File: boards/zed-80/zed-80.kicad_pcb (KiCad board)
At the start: 2 copper layers, 31 parts, among them J401 TYPE-C-31-M-12, SW201 SW_Push, U201 GD74LS04, U202 Z84C0010PEC, U301 TT74LS32BI, U302 AT28C256-15PU, U303 HM628128BLP-10, U401 CH340C, U402 MC68B50P, Y201 7.3728 MHz

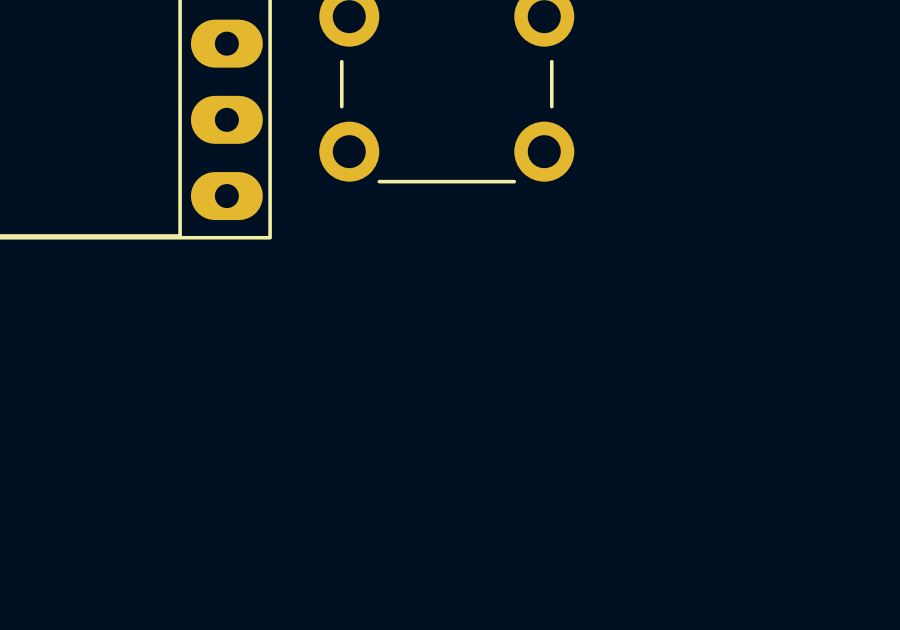
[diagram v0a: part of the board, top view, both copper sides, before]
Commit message: New zed-80 revision and initial ROM programmer schematic
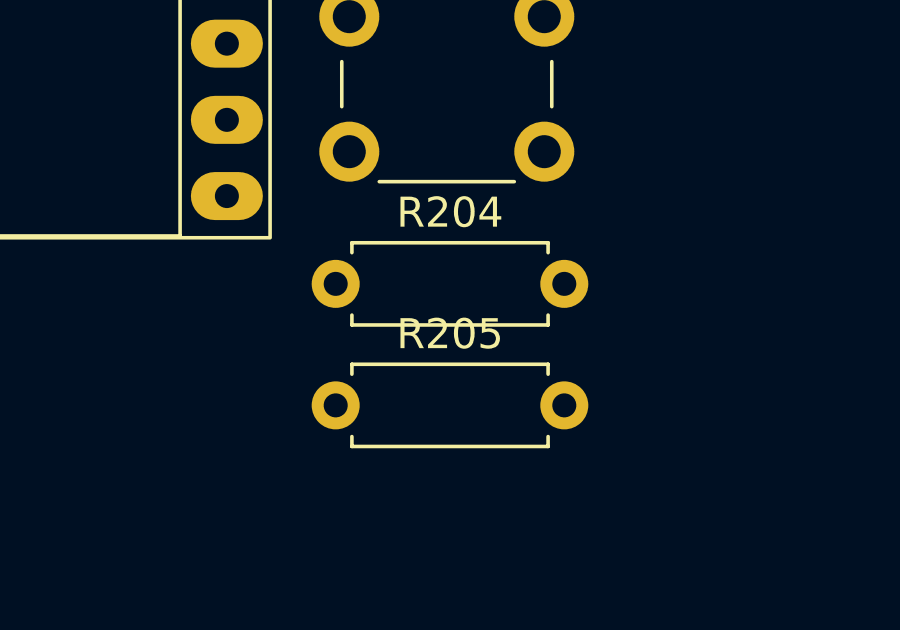
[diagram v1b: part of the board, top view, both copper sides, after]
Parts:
- added R204: 10 kΩ, Resistor_THT:R_Axial_DIN0207_L6.3mm_D2.5mm_P7.62mm_Horizontal, F.Cu at (104.9, 101.5)
- added R205: 1 kΩ, Resistor_THT:R_Axial_DIN0207_L6.3mm_D2.5mm_P7.62mm_Horizontal, F.Cu at (104.9, 105.5)
- R201: value 1 MΩ -> 2 kΩ
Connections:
- U401 pad 15: unconnected-(U401-R232-Pad15) -> GND
- U402 pad 23: unconnected-(U402-~{DCD}-Pad23) -> GND
- U402 pad 24: unconnected-(U402-~{CTS}-Pad24) -> GND

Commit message: Initial layout for main board
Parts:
- moved MH101 97.5 mm to (85.0, 45.0)
- moved J401 84.4 mm to (82.4, 71.2), turned to -90 degrees
- moved MH103 82.9 mm to (85.0, 107.5)
- moved D401 77.1 mm to (84.2, 82.2), turned to -90 degrees
- moved R401 75.0 mm to (83.8, 63.6), turned to 90 degrees
- moved R402 73.5 mm to (88.8, 63.6), turned to 90 degrees
- moved U401 66.6 mm to (95.0, 71.5), turned to -90 degrees
- moved R403 62.5 mm to (91.2, 83.2)
- moved MH102 61.2 mm to (182.5, 45.0)
- moved C402 60.6 mm to (94.0, 66.0)
- moved U301 59.5 mm to (120.2, 89.4)
- moved R203 58.1 mm to (169.1, 93.0), turned to 180 degrees
- moved SW201 56.9 mm to (162.0, 97.5)
- moved U202 56.3 mm to (142.3, 51.4)
- moved C401 54.5 mm to (93.5, 77.2)
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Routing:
- net /CPU/A0: track 0.00 -> 63.3 mm
- net /CPU/A6: track 0.00 -> 42.2 mm
- net /CPU/A4: track 0.00 -> 42.2 mm
- net /CPU/A2: track 0.00 -> 42.2 mm
- net /CPU/A5: track 0.00 -> 42.2 mm
- net /CPU/A1: track 0.00 -> 42.2 mm
- net /CPU/A3: track 0.00 -> 42.2 mm
- net Net-(C201-Pad1): track 0.00 -> 33.3 mm
- net /CPU/D1: track 0.00 -> 21.1 mm
- net /CPU/D0: track 0.00 -> 21.1 mm
- net /CPU/A8: track 0.00 -> 21.1 mm
- net /CPU/CLK: track 0.00 -> 14.2 mm
- net Net-(C202-Pad1): track 0.00 -> 13.1 mm
- net Net-(R201-Pad2): track 0.00 -> 9.56 mm
- net /CPU/A7: track 0.00 -> 5.96 mm
- added copper zone on B.Cu, net GND
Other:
- board outline added: 107.5 x 72.5 mm

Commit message: Initial PCB design for main board
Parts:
- moved U302 39.2 mm to (161.1, 56.5)
- moved U301 39.2 mm to (155.6, 106.1), turned to 90 degrees
- moved C302 35.7 mm to (168.5, 51.5)
- moved R204 28.6 mm to (110.9, 84.8), turned to 0 degrees
- moved C301 27.5 mm to (160.2, 93.5), turned to 180 degrees
- moved U303 20.8 mm to (141.6, 51.5)
- moved U202 20.1 mm to (122.1, 51.4)
- moved C203 20.0 mm to (121.7, 103.2)
- moved SW201 19.5 mm to (142.5, 98.5)
- moved R203 19.5 mm to (149.6, 93.5)
- moved R205 15.2 mm to (116.2, 100.8), turned to 90 degrees
- moved C204 13.6 mm to (105.5, 105.8), turned to 0 degrees
- moved C303 8.39 mm to (165.5, 51.5), turned to 180 degrees
- moved MH102 5.59 mm to (177.5, 47.5)
- moved R401 5.25 mm to (89.0, 63.6)
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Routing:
- net VBUS: track 0.00 -> 278.4 mm, vias 0 -> 2
- net /CPU/A13: track 0.00 -> 102.4 mm, vias 0 -> 4
- net /CPU/A15: track 0.00 -> 94.1 mm, vias 0 -> 3
- net /CPU/A14: track 0.00 -> 86.3 mm, vias 0 -> 2
- net /CPU/D3: track 0.00 -> 84.3 mm, vias 0 -> 2
- net /CPU/D4: track 0.00 -> 76.4 mm, vias 0 -> 2
- net /CPU/D7: track 0.00 -> 75.6 mm, vias 0 -> 4
- net /Memory/~{ROM}: track 0.00 -> 75.1 mm, vias 0 -> 1
- net /CPU/D2: track 0.00 -> 72.1 mm, vias 0 -> 1
- net /CPU/A11: track 0.00 -> 69.6 mm, vias 0 -> 2
- net /CPU/A7: track 5.96 -> 75.1 mm, vias 0 -> 2
- net /CPU/D5: track 0.00 -> 68.9 mm, vias 0 -> 3
- net /CPU/CLK: track 14.2 -> 82.6 mm, vias 0 -> 1
- net /CPU/~{WR}: track 0.00 -> 66.6 mm, vias 0 -> 2
- net /CPU/D6: track 0.00 -> 66.1 mm, vias 0 -> 2
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- added copper zone on F.Cu, net GND
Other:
- board size 107.5 x 72.5 mm -> 102.5 x 70 mm

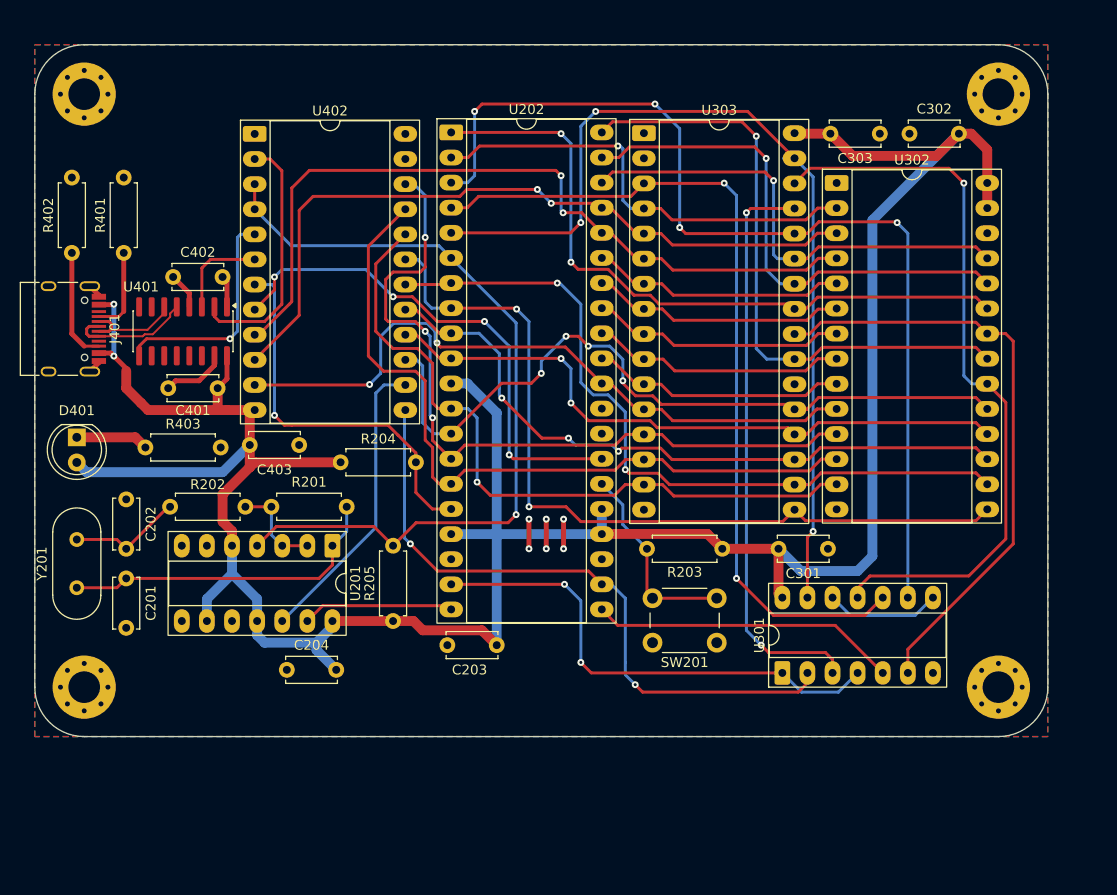
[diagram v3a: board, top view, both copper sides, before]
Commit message: Fixed DRC errors and added silkscreens
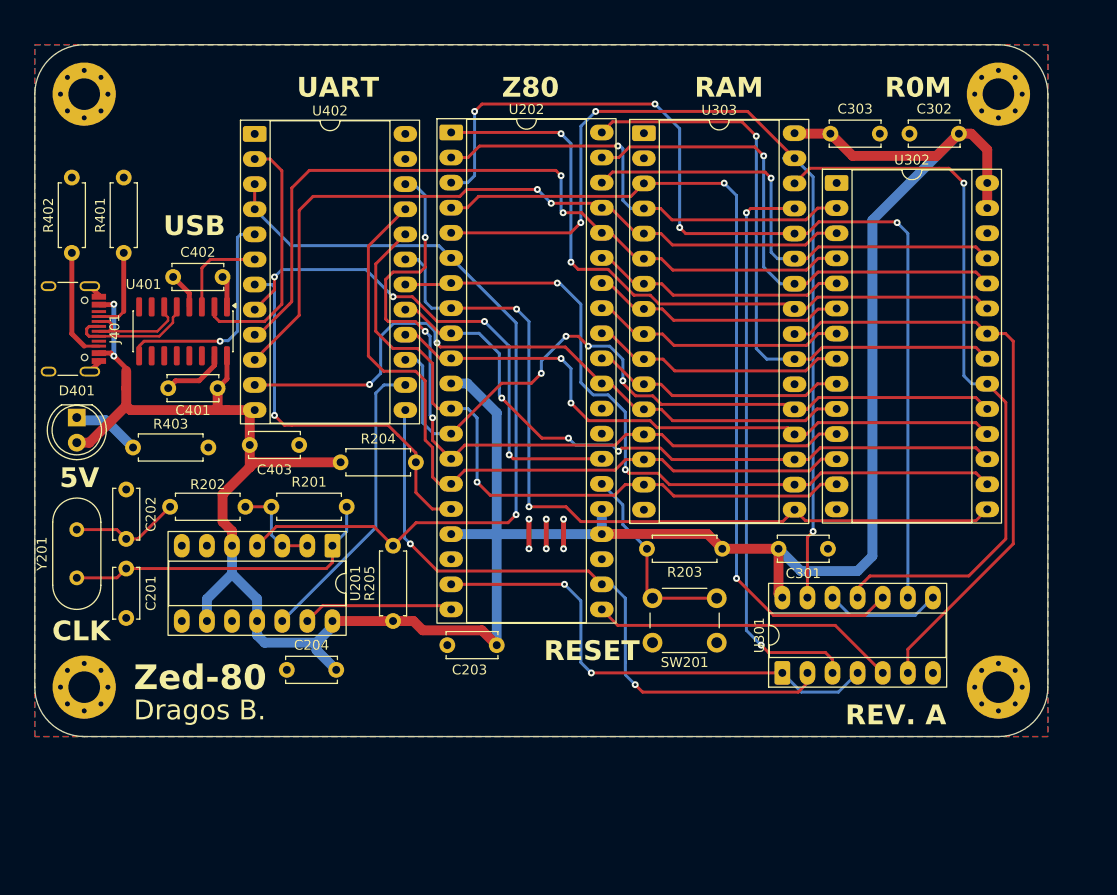
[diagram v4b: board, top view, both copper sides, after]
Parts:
- moved D401 2.00 mm to (84.2, 80.2)
- moved R403 1.25 mm to (89.9, 83.2)
- moved C201 1.00 mm to (89.2, 95.5)
- moved C202 1.00 mm to (89.2, 92.5)
- moved Y201 1.00 mm to (84.2, 96.4)
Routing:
- net VBUS: track 278.4 -> 266.9 mm
- net /USB-to-UART/D-: track 11.2 -> 12.2 mm
- net Net-(C201-Pad1): track 33.3 -> 32.7 mm
- net /USB-to-UART/D+: track 12.5 -> 13.0 mm
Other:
- rule pad_to_mask_clearance: 0.1 -> 0
- board text added: "5V"
- board text added: "CLK"
- board text added: "Dragos B."
- board text added: "R0M"
- board text added: "RAM"
- board text added: "RESET"
- board text added: "REV. A"
- board text added: "UART"
- board text added: "USB"
- board text added: "Z80"
- board text added: "Zed-80"

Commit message: Fixed small issues and added QR code to main board
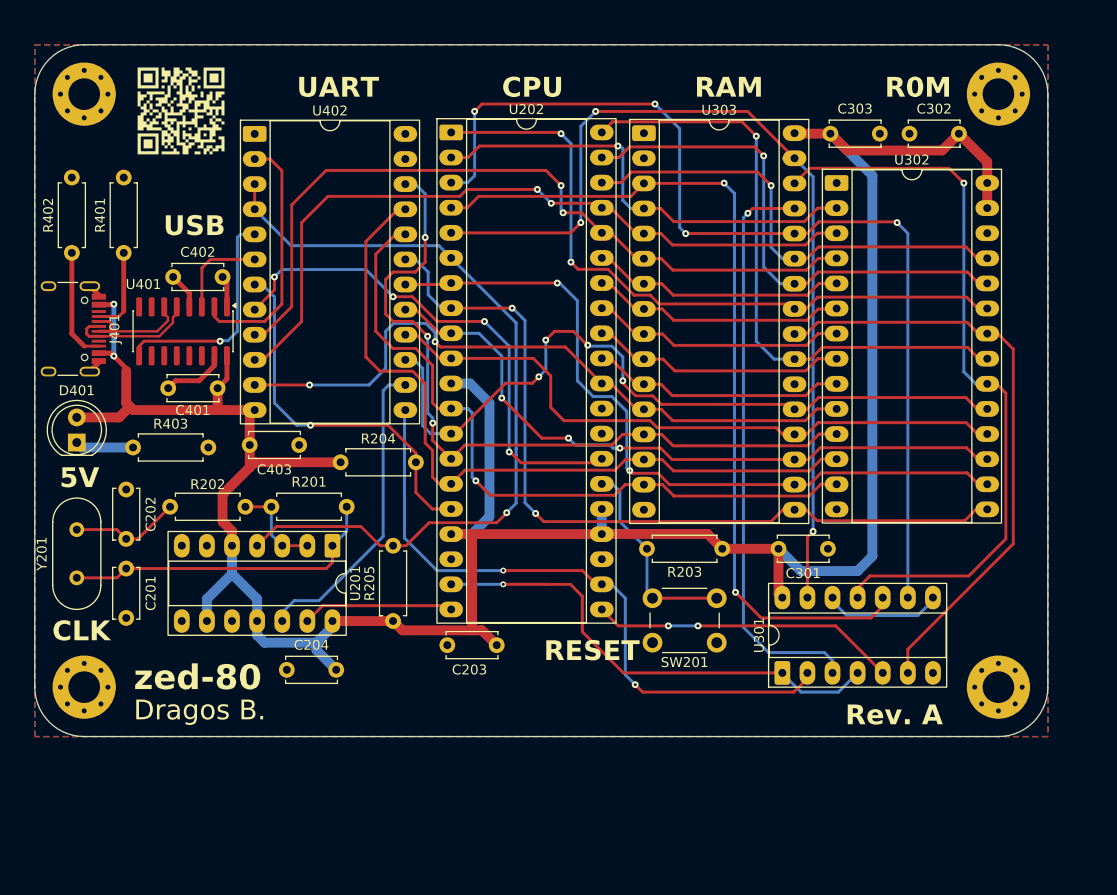
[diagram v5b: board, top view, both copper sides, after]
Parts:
- added G***: LOGO, custom:qr, F.Cu at (94.8, 49.2)
- moved D401 2.53 mm to (84.2, 82.8), turned to 90 degrees
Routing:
- net GND: track 21.7 -> 12.7 mm, vias 6 -> 0
- net VBUS: track 266.9 -> 264.1 mm
- net /CPU/D7: track 75.6 -> 77.2 mm
- net /CPU/A14: track 86.3 -> 87.9 mm
- net Net-(U402-E): track 30.3 -> 31.9 mm
- net /CPU/~{MREQ}: track 50.1 -> 48.6 mm, vias 2 -> 1
- net /CPU/~{INT}: track 39.2 -> 37.9 mm
- net /CPU/A6: track 79.3 -> 78.0 mm
- net Net-(D401-K): track 6.94 -> 5.90 mm
- net /CPU/D3: track 84.3 -> 83.5 mm
- net /CPU/A8: track 48.4 -> 47.7 mm
- net /CPU/CLK: track 82.6 -> 82.0 mm
- net /CPU/D1: track 76.4 -> 77.1 mm
- net /CPU/D0: track 77.8 -> 77.1 mm
- net /CPU/~{RST}: track 20.2 -> 20.8 mm
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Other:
- board text added: "CPU"
- board text added: "Rev. A"
- board text added: "zed-80"
- board text removed: "REV. A"
- board text removed: "Z80"
- board text removed: "Zed-80"

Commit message: Small fixup of main board
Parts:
- moved G*** 0.30 mm to (94.5, 49.2)
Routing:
- net /CPU/A7: track 74.7 -> 71.6 mm
- net /CPU/D7: track 77.2 -> 74.2 mm
- net /CPU/~{WR}: track 66.4 -> 63.6 mm
- net /CPU/A6: track 78.0 -> 75.4 mm
- net Net-(U402-E): track 31.9 -> 29.8 mm
- net /CPU/D3: track 83.5 -> 81.4 mm
- net /Memory/~{ROM}: track 75.4 -> 73.5 mm
- net /CPU/A4: track 25.8 -> 24.1 mm
- net /CPU/A1: track 25.8 -> 24.2 mm
- net /CPU/A0: track 68.8 -> 67.1 mm
- net /CPU/A5: track 25.8 -> 24.2 mm
- net /CPU/A3: track 25.8 -> 24.2 mm
- net /CPU/A2: track 25.8 -> 24.2 mm
- net /CPU/A11: track 69.6 -> 68.0 mm
- net /CPU/A15: track 94.1 -> 93.0 mm
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
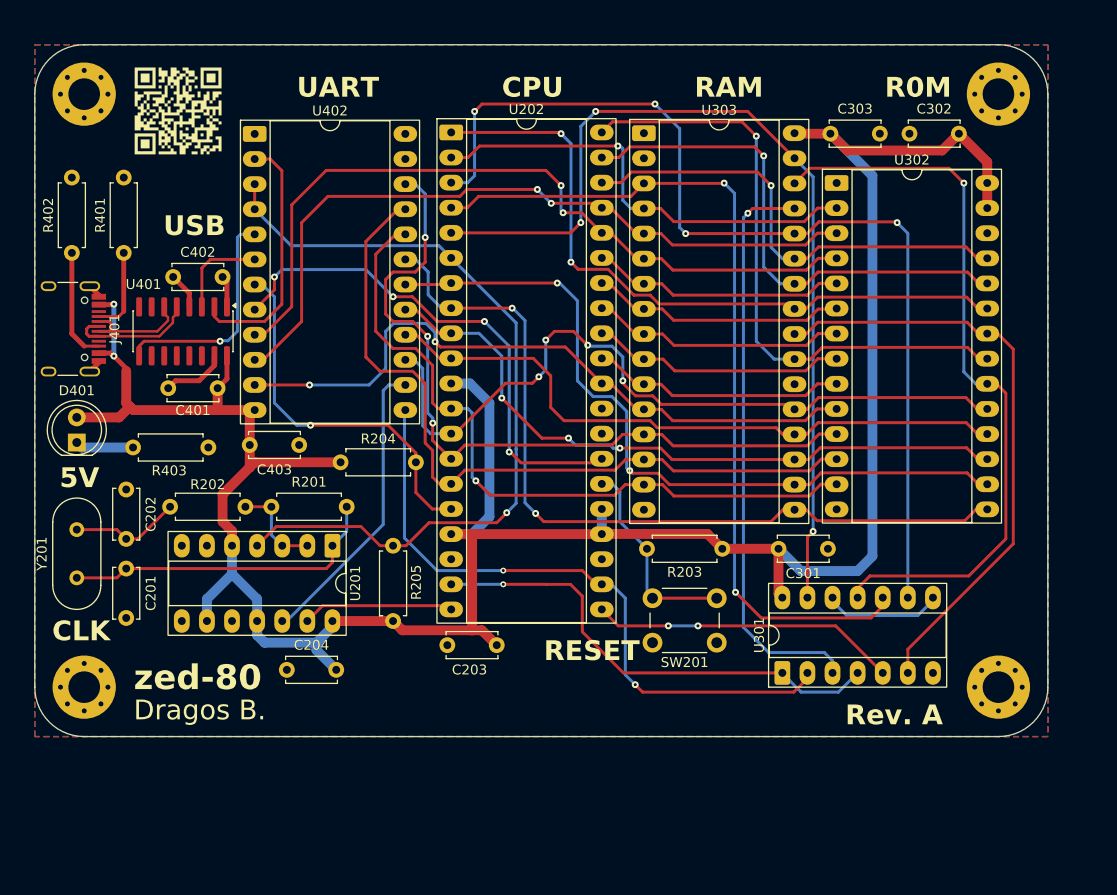
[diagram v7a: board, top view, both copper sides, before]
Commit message: Fixed QR code library linking
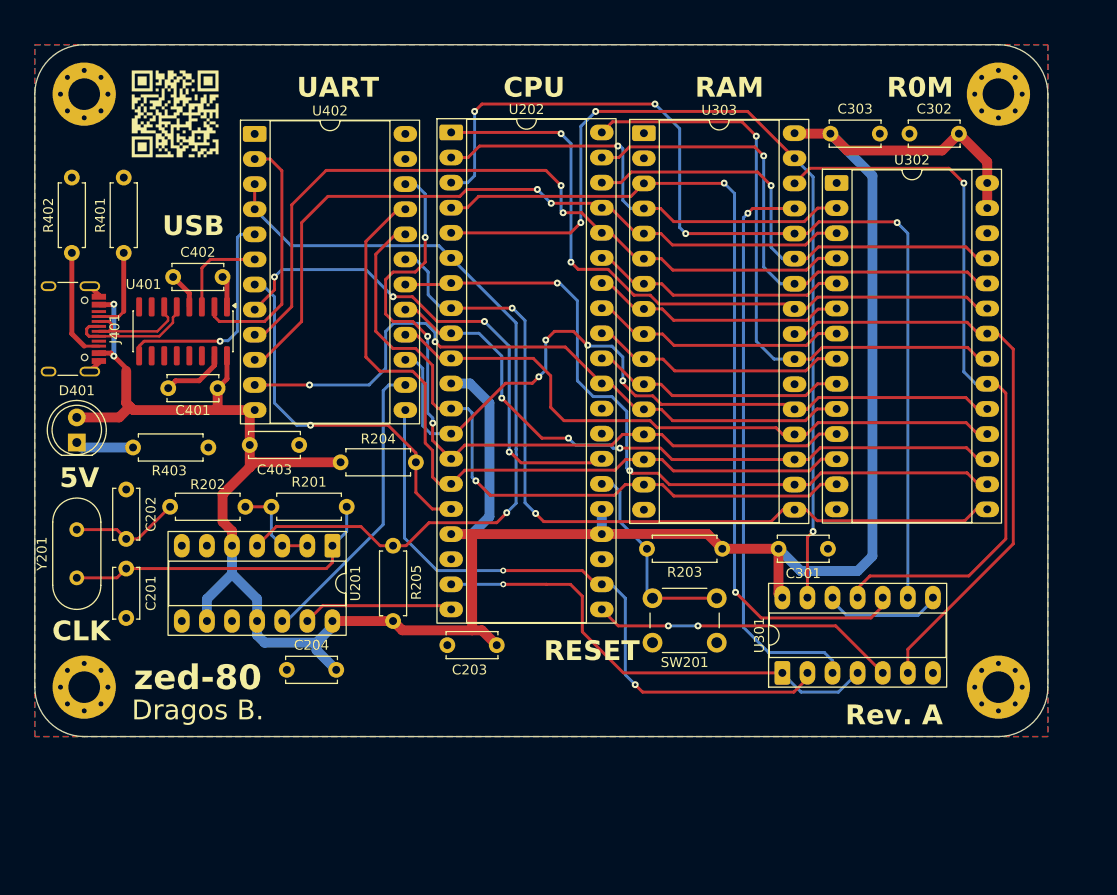
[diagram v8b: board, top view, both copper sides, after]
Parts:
- removed the G*** at (94.5, 49.2)
- added G***: LOGO, code:qr, F.Cu at (94.2, 49.5)
